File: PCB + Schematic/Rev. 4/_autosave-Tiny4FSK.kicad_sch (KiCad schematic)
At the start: 90 parts, among them IC1 SI4063, J1 SWD, J10 USB, J2 GPIO, J3 USBC, J4 USB, J5 I2C, J6 Power, J7 SPI, J8 USB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

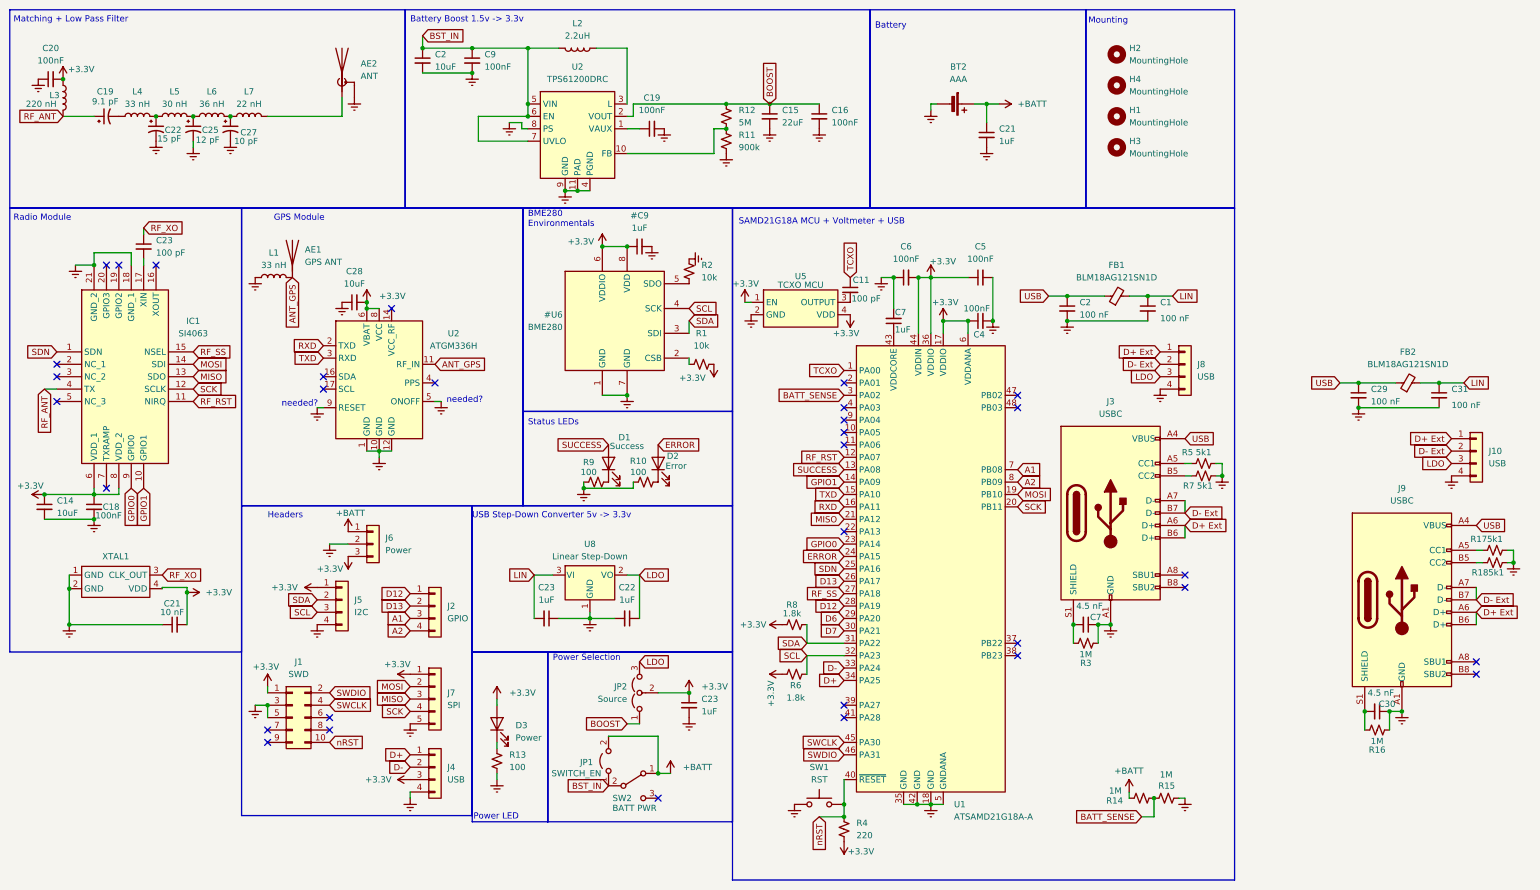
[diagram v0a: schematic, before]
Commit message: USB Breakout, PCB further along
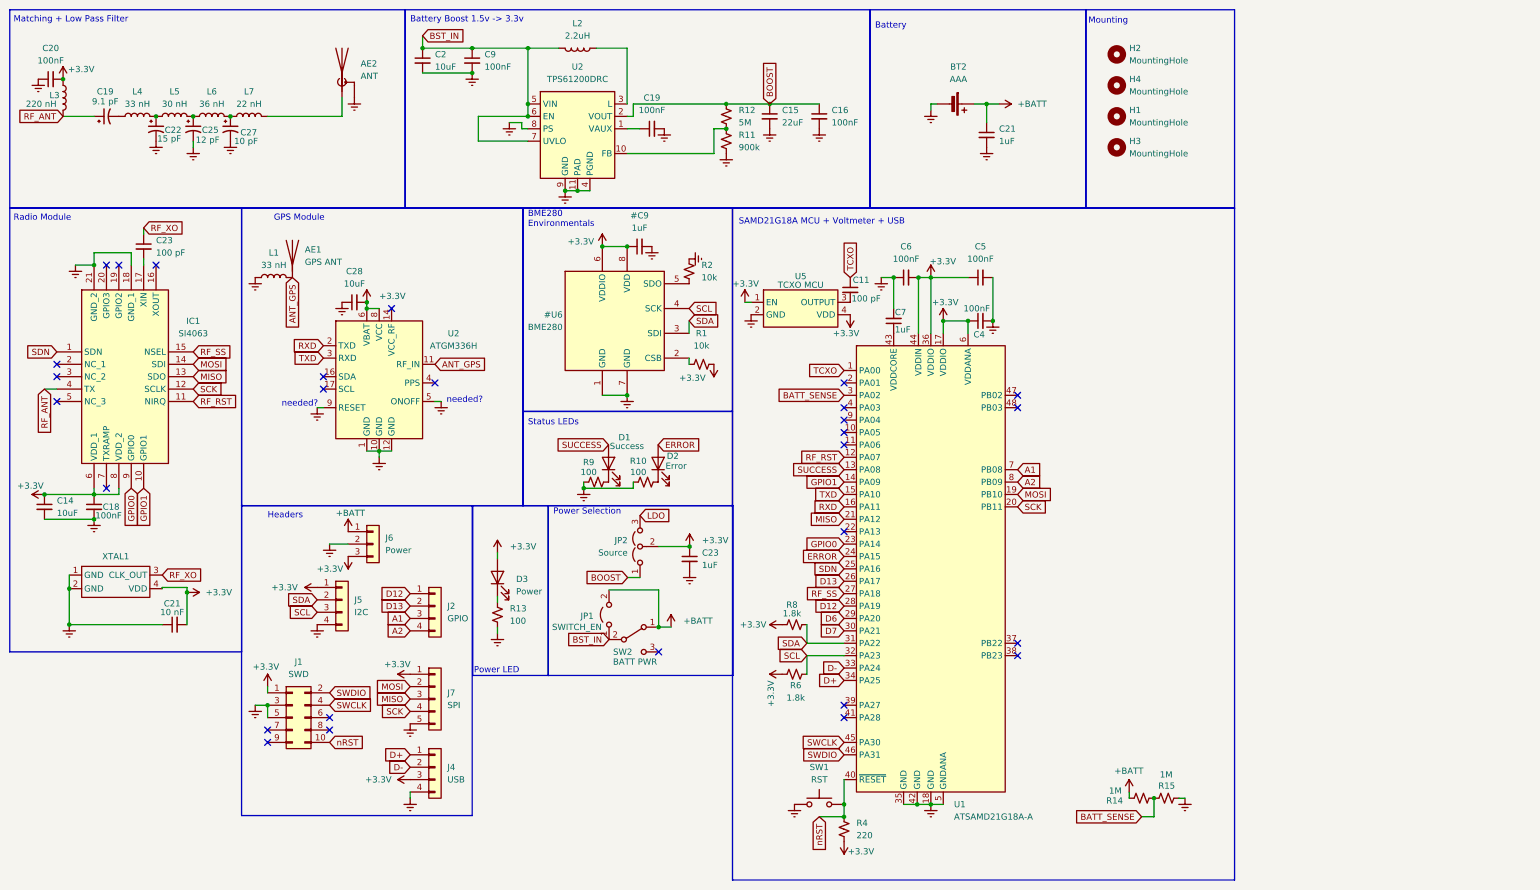
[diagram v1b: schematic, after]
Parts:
- removed C1, C2, C29, C31: 100 nF, Capacitor_SMD:C_0805_2012Metric_Pad1.18x1.45mm_HandSolder, symbol Device:C_Small
- removed C22, C23: 1uF, Capacitor_SMD:C_0805_2012Metric_Pad1.18x1.45mm_HandSolder, symbol Device:C_Small
- removed C30, C7: 4.5 nF, Capacitor_SMD:C_0805_2012Metric_Pad1.18x1.45mm_HandSolder, symbol Device:C_Small
- removed FB1, FB2: BLM18AG121SN1D, Resistor_SMD:R_0603_1608Metric_Pad0.98x0.95mm_HandSolder, symbol Device:FerriteBead_Small
- removed J10, J8: USB, Connector_PinHeader_2.54mm:PinHeader_1x04_P2.54mm_Vertical, symbol Connector_Generic:Conn_01x04
- removed J3, J9: USBC, Connector_USB:USB_C_Receptacle_GCT_USB4105-xx-A_16P_TopMnt_Horizontal, symbol Connector:USB_C_Receptacle_USB2.0
- removed R16, R3: 1M, Resistor_SMD:R_0805_2012Metric_Pad1.20x1.40mm_HandSolder, symbol Device:R_Small_US
- removed R17, R18, R5, R7: 5k1, Resistor_SMD:R_0805_2012Metric_Pad1.20x1.40mm_HandSolder, symbol Device:R_Small_US
- removed U8: Linear Step-Down, LDO:MCP1700, symbol Regulator_Linear:MCP1700x-330xxTT
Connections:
- no-connect marks 32 -> 28
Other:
- note removed: "USB Step-Down Converter 5v -> 3.3v"
- moved on the sheet: C23, D3, JP1, JP2, R13, SW2

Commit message: Expansion GPIO
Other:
- moved on the sheet: C11, R14, R15, U5
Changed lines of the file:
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@@
 	)
 	(junction
-		(at 248.92 177.8)
+		(at 248.92 147.32)
 		(diameter 0)
 		(color 0 0 0 0)
@@
 	(wire
 		(pts
-			(xy 248.92 177.8) (xy 248.92 181.61)
+			(xy 248.92 147.32) (xy 248.92 151.13)
 		)
 		(stroke
@@
 	(wire
 		(pts
-			(xy 246.38 181.61) (xy 248.92 181.61)
+			(xy 246.38 151.13) (xy 248.92 151.13)
 		)
 		(stroke
@@
 	(wire
 		(pts
-			(xy 243.84 176.53) (xy 243.84 177.8)
+			(xy 243.84 146.05) (xy 243.84 147.32)
 		)
 		(stroke
@@
 	(wire
 		(pts
-			(xy 165.1 76.2) (xy 166.37 76.2)
+			(xy 236.22 121.92) (xy 237.49 121.92)
 		)
 		(stroke
@@
 	(wire
 		(pts
-			(xy 255.27 177.8) (xy 254 177.8)
+			(xy 255.27 147.32) (xy 254 147.32)
 		)
 		(stroke
@@
 	(global_label "TCXO"
 		(shape input)
-		(at 186.69 71.12 90)
+		(at 257.81 116.84 90)
 		(fields_autoplaced yes)
 		(effects
@@
 		)
 		(property "Intersheetrefs" "${INTERSHEET_REFS}"
-			(at 186.69 63.3572 90)
+			(at 257.81 109.0772 90)
 			(effects
 				(font
@@
 	(global_label "BATT_SENSE"
 		(shape input)
-		(at 246.38 181.61 180)
+		(at 246.38 151.13 180)
 		(fields_autoplaced yes)
 		(effects
@@
 		)
 		(property "Intersheetrefs" "${INTERSHEET_REFS}"
-			(at 232.0859 181.61 0)
+			(at 232.0859 151.13 0)
 			(effects
 				(font
@@
 	(symbol
 		(lib_id "Oscillator:ATXK-H11-E-32.768KHZ-E50-T3")
-		(at 176.53 72.39 0)
+		(at 247.65 118.11 0)
 		(unit 1)
 		(exclude_from_sim no)
@@
 		(dnp no)
 		(property "Reference" "U5"
-			(at 176.53 70.866 0)
+			(at 247.65 116.586 0)
 			(effects
 				(font
@@
 		)
 		(property "Value" "TCXO MCU"
-			(at 176.53 72.644 0)
+			(at 247.65 118.364 0)
 			(effects
 				(font
@@
 		)
 		(property "Footprint" "Oscillator_TCXO:ATXK-H11-E-32.768KHZ-E50-T3"
-			(at 176.53 72.39 0)
+			(at 247.65 118.11 0)
 			(effects
 				(font
@@
 		)
 		(property "Datasheet" ""
-			(at 176.53 72.39 0)
+			(at 247.65 118.11 0)
 			(effects
 				(font
@@
 		)
 		(property "Description" ""
-			(at 176.53 72.39 0)
+			(at 247.65 118.11 0)
 			(effects
 				(font
@@
 		(lib_name "+3.3V_6")
 		(lib_id "power:+3.3V")
-		(at 165.1 76.2 0)
+		(at 236.22 121.92 0)
 		(unit 1)
 		(exclude_from_sim no)
@@
 		(dnp no)
 		(property "Reference" "#PWR051"
-			(at 165.1 80.01 0)
+			(at 236.22 125.73 0)
 			(effects
 				(font
@@
 		)
 		(property "Value" "+3.3V"
-			(at 162.56 72.39 0)
+			(at 233.68 118.11 0)
 			(effects
 				(font
@@
 		)
 		(property "Footprint" ""
-			(at 165.1 76.2 0)
+			(at 236.22 121.92 0)
 			(effects
 				(font
@@
 		)
 		(property "Datasheet" ""
-			(at 165.1 76.2 0)
+			(at 236.22 121.92 0)
 			(effects
 				(font
@@
 		)
 		(property "Description" ""
-			(at 165.1 76.2 0)
+			(at 236.22 121.92 0)
 			(effects
 				(font
@@
 		(lib_name "Earth_4")
 		(lib_id "power:Earth")
-		(at 255.27 177.8 0)
+		(at 255.27 147.32 0)
 		(unit 1)
 		(exclude_from_sim no)
@@
 		(fields_autoplaced yes)
 		(property "Reference" "#PWR053"
-			(at 255.27 184.15 0)
+			(at 255.27 153.67 0)
 			(effects
 				(font
@@
 		)
 		(property "Value" "Earth"
-			(at 255.27 181.61 0)
+			(at 255.27 151.13 0)
 			(effects
 				(font
@@
 		)
 		(property "Footprint" ""
-			(at 255.27 177.8 0)
+			(at 255.27 147.32 0)
 			(effects
 				(font
@@
 		)
 		(property "Datasheet" "~"
-			(at 255.27 177.8 0)
+			(at 255.27 147.32 0)
 			(effects
 				(font
@@
 		)
 		(property "Description" ""
-			(at 255.27 177.8 0)
+			(at 255.27 147.32 0)
 			(effects
 				(font
@@
 	(symbol
 		(lib_id "Device:R_Small_US")
-		(at 251.46 177.8 90)
+		(at 251.46 147.32 90)
 		(unit 1)
 		(exclude_from_sim no)
@@
 		(dnp no)
 		(property "Reference" "R15"
-			(at 253.238 175.26 90)
+			(at 253.238 144.78 90)
 			(effects
 				(font
@@
 		)
 		(property "Value" "1M"
-			(at 252.73 172.974 90)
+			(at 252.73 142.494 90)
 			(effects
 				(font
@@
 		)
 		(property "Footprint" "Resistor_SMD:R_0805_2012Metric_Pad1.20x1.40mm_HandSolder"
-			(at 251.46 177.8 0)
+			(at 251.46 147.32 0)
 			(effects
 				(font
@@
 		)
 		(property "Datasheet" "~"
-			(at 251.46 177.8 0)
+			(at 251.46 147.32 0)
 			(effects
 				(font
@@
 		)
 		(property "Description" "Resistor, small US symbol"
-			(at 251.46 177.8 0)
+			(at 251.46 147.32 0)
 			(effects
 				(font
@@
 		(lib_name "Earth_4")
 		(lib_id "power:Earth")
-		(at 166.37 78.74 0)
+		(at 237.49 124.46 0)
 		(unit 1)
 		(exclude_from_sim no)
@@
 		(fields_autoplaced yes)
 		(property "Reference" "#PWR026"
-			(at 166.37 85.09 0)
+			(at 237.49 130.81 0)
 			(effects
 				(font
@@
 		)
 		(property "Value" "Earth"
-			(at 166.37 82.55 0)
+			(at 237.49 128.27 0)
 			(effects
 				(font
@@
 		)
 		(property "Footprint" ""
-			(at 166.37 78.74 0)
+			(at 237.49 124.46 0)
 			(effects
 				(font
@@
 		)
 		(property "Datasheet" "~"
-			(at 166.37 78.74 0)
+			(at 237.49 124.46 0)
 			(effects
 				(font
@@
 		)
 		(property "Description" ""
-			(at 166.37 78.74 0)
+			(at 237.49 124.46 0)
 			(effects
 				(font
@@
 		(lib_name "+3.3V_6")
 		(lib_id "power:+3.3V")
-		(at 186.69 78.74 180)
+		(at 257.81 124.46 180)
 		(unit 1)
 		(exclude_from_sim no)
@@
 		(dnp no)
 		(property "Reference" "#PWR050"
-			(at 186.69 74.93 0)
+			(at 257.81 120.65 0)
 			(effects
 				(font
@@
 		)
 		(property "Value" "+3.3V"
-			(at 183.134 82.55 0)
+			(at 254.254 128.27 0)
 			(effects
 				(font
@@
 		)
 		(property "Footprint" ""
-			(at 186.69 78.74 0)
+			(at 257.81 124.46 0)
 			(effects
 				(font
@@
 		)
 		(property "Datasheet" ""
-			(at 186.69 78.74 0)
+			(at 257.81 124.46 0)
 			(effects
 				(font
@@
 		)
 		(property "Description" ""
-			(at 186.69 78.74 0)
+			(at 257.81 124.46 0)
 			(effects
 				(font
@@
 		(lib_name "+BATT_1")
 		(lib_id "power:+BATT")
-		(at 243.84 176.53 0)
+		(at 243.84 146.05 0)
 		(unit 1)
 		(exclude_from_sim no)
@@
 		(dnp no)
 		(property "Reference" "#PWR055"
-			(at 243.84 180.34 0)
+			(at 243.84 149.86 0)
 			(effects
 				(font
@@
 		)
 		(property "Value" "+BATT"
-			(at 240.792 172.212 0)
+			(at 240.792 141.732 0)
 			(effects
 				(font
@@
 		)
 		(property "Footprint" ""
-			(at 243.84 176.53 0)
+			(at 243.84 146.05 0)
 			(effects
 				(font
@@
 		)
 		(property "Datasheet" ""
-			(at 243.84 176.53 0)
+			(at 243.84 146.05 0)
 			(effects
 				(font
@@
 		)
 		(property "Description" ""
-			(at 243.84 176.53 0)
+			(at 243.84 146.05 0)
 			(effects
 				(font
@@
 	(symbol
 		(lib_id "Device:R_Small_US")
-		(at 246.38 177.8 90)
+		(at 246.38 147.32 90)
 		(unit 1)
 		(exclude_from_sim no)
@@
 		(dnp no)
 		(property "Reference" "R14"
-			(at 242.57 178.308 90)
+			(at 242.57 147.828 90)
 			(effects
 				(font
@@
 		)
 		(property "Value" "1M"
-			(at 242.316 176.276 90)
+			(at 242.316 145.796 90)
 			(effects
 				(font
@@
 		)
 		(property "Footprint" "Resistor_SMD:R_0805_2012Metric_Pad1.20x1.40mm_HandSolder"
-			(at 246.38 177.8 0)
+			(at 246.38 147.32 0)
 			(effects
 				(font
@@
 		)
 		(property "Datasheet" "~"
-			(at 246.38 177.8 0)
+			(at 246.38 147.32 0)
 			(effects
 				(font
@@
 		)
 		(property "Description" "Resistor, small US symbol"
-			(at 246.38 177.8 0)
+			(at 246.38 147.32 0)
 			(effects
 				(font
@@
 	(symbol
 		(lib_id "Device:C_Small")
-		(at 186.69 73.66 0)
+		(at 257.81 119.38 0)
 		(unit 1)
 		(exclude_from_sim no)
@@
 		(dnp no)
 		(property "Reference" "C11"
-			(at 187.198 71.628 0)
+			(at 258.318 117.348 0)
 			(effects
 				(font
@@
 		)
 		(property "Value" "100 pF"
-			(at 186.944 75.438 0)
+			(at 258.064 121.158 0)
 			(effects
 				(font
@@
 		)
 		(property "Footprint" "Capacitor_SMD:C_0805_2012Metric_Pad1.18x1.45mm_HandSolder"
-			(at 186.69 73.66 0)
+			(at 257.81 119.38 0)
 			(effects
 				(font
@@
 		)
 		(property "Datasheet" "~"
-			(at 186.69 73.66 0)
+			(at 257.81 119.38 0)
 			(effects
 				(font
@@
 		)
 		(property "Description" "Unpolarized capacitor, small symbol"
-			(at 186.69 73.66 0)
+			(at 257.81 119.38 0)
 			(effects
 				(font
